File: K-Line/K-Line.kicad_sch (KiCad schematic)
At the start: 26 parts, among them J1 Conn_01x10_Pin, Q1 Q_NMOS_GSD, Q2 Q_NMOS_GSD, Q3 Q_NMOS_GSD, Q4 Q_NMOS_GSD, U1 ESP32-C3 SuperMini, U2 Mini-560, U3 ER_OLEDM0.91_1x-I2C

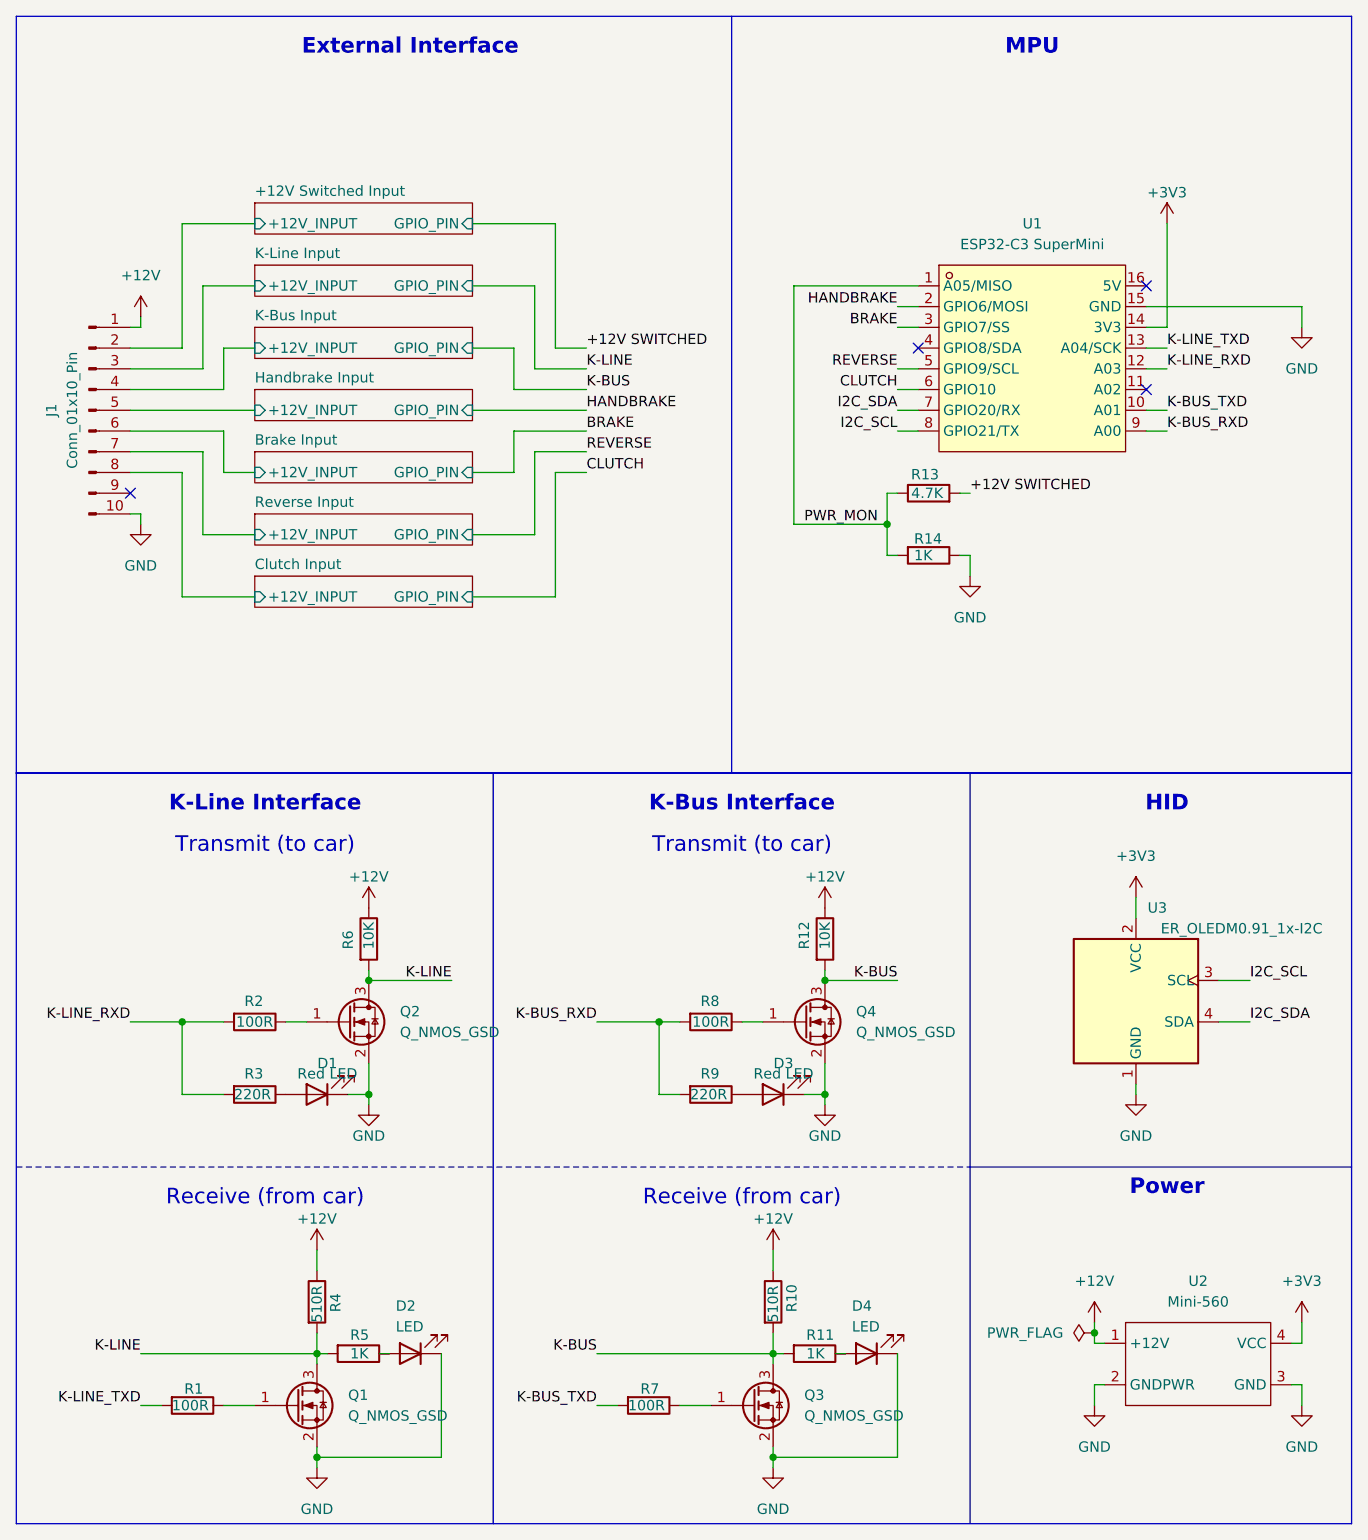
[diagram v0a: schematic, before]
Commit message: Simplify K-Line & K-Bus read/write
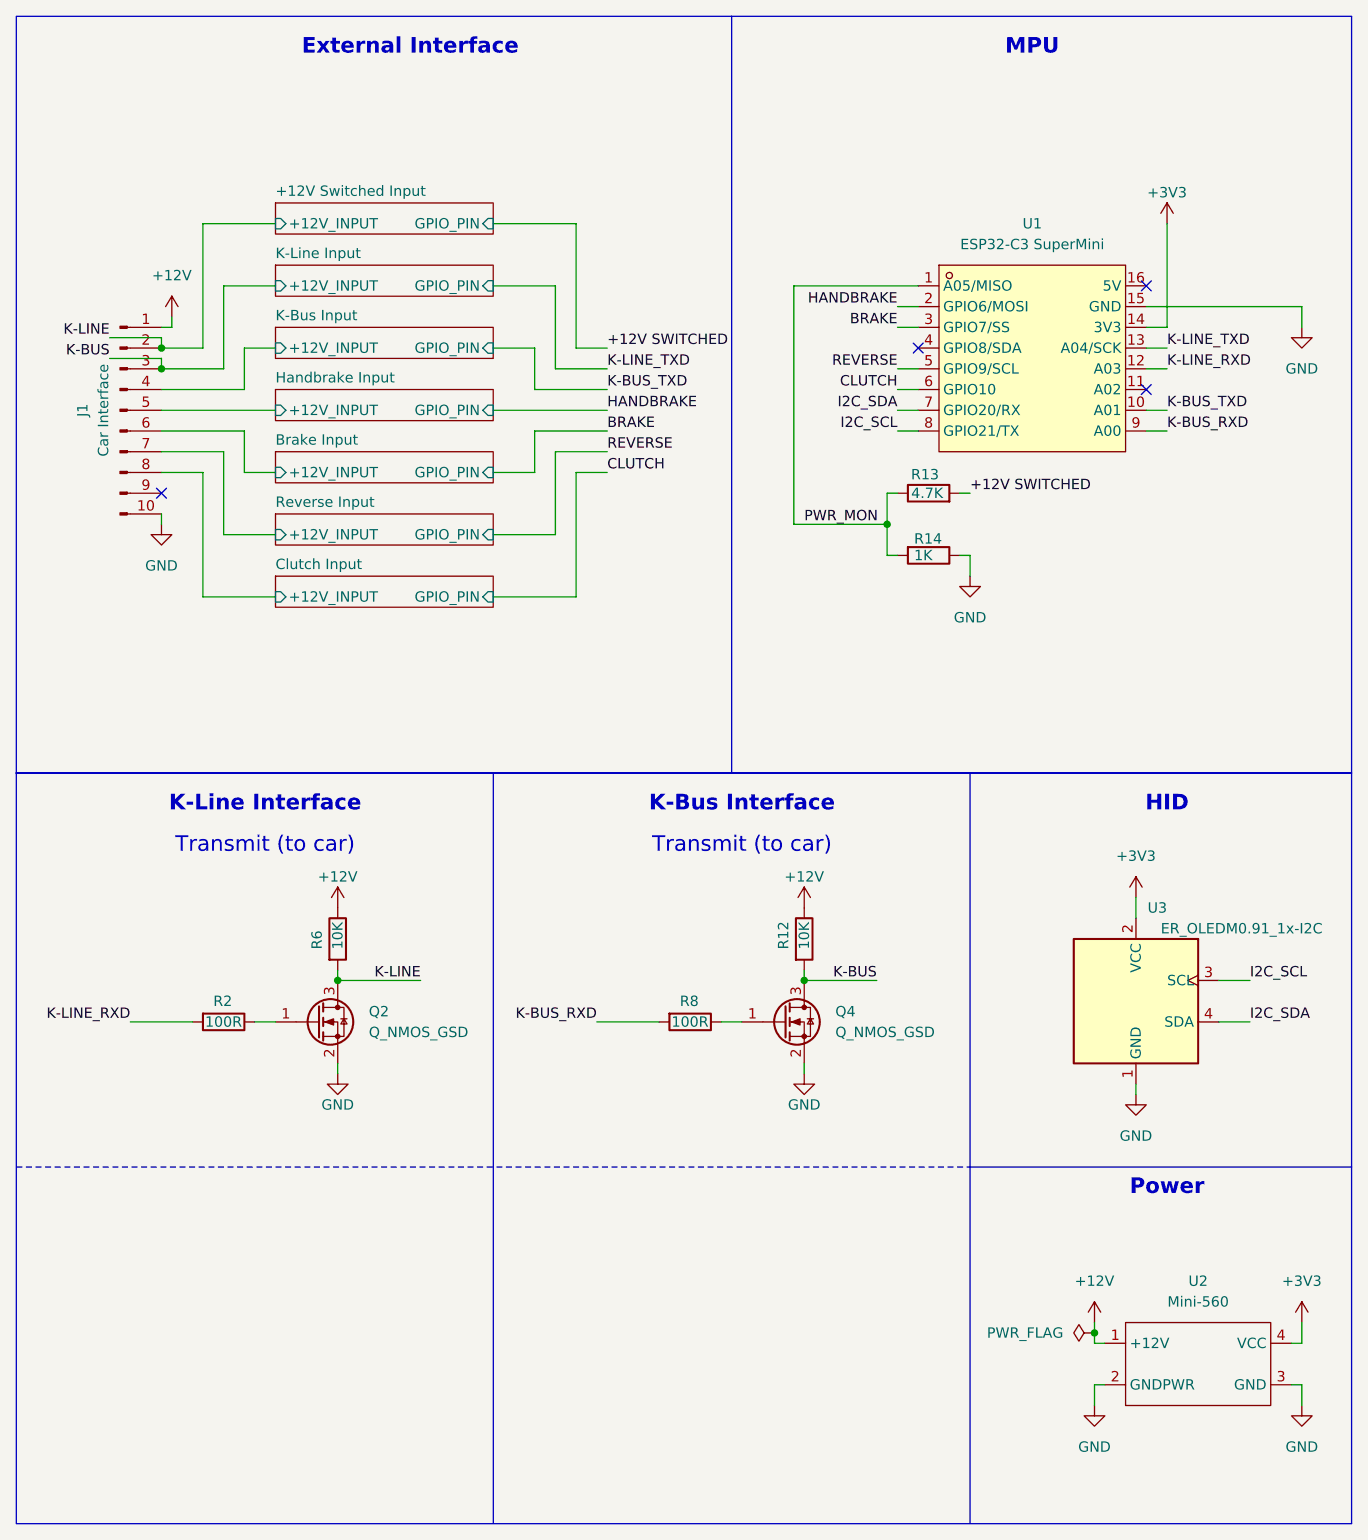
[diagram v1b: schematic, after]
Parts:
- removed D1, D3: Red LED, LED_SMD:LED_1206_3216Metric_Pad1.42x1.75mm_HandSolder, symbol Device:LED
- removed D2, D4: LED, LED_SMD:LED_1206_3216Metric_Pad1.42x1.75mm_HandSolder, symbol Device:LED
- removed Q1, Q3: Q_NMOS_GSD, Package_TO_SOT_SMD:SC-59_Handsoldering, symbol Transistor_FET:Q_NMOS_GSD
- removed R1, R7: 100R, Resistor_SMD:R_1206_3216Metric_Pad1.30x1.75mm_HandSolder, symbol Device:R
- removed R10, R4: 510R, Resistor_SMD:R_1206_3216Metric_Pad1.30x1.75mm_HandSolder, symbol Device:R
- removed R11, R5: 1K, Resistor_SMD:R_1206_3216Metric_Pad1.30x1.75mm_HandSolder, symbol Device:R
- removed R3, R9: 220R, Resistor_SMD:R_1206_3216Metric_Pad1.30x1.75mm_HandSolder, symbol Device:R
- J1: value Conn_01x10_Pin -> Car Interface
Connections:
- net +12V Switched Input/+12V_INPUT is gone; now on net K-LINE: J1.2 (Pin_2)
- net K-Line Input/+12V_INPUT is gone; now on net K-BUS: J1.3 (Pin_3)
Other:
- note removed: "Receive (from car)"
- moved on the sheet: J1, Q2, Q4, R12, R2, R6, R8
